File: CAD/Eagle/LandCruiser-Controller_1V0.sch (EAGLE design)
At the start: 56 parts, among them K311 V23086C1001A403, K312 V23086C1001A403, K313 V23086C1001A403, K314 V23086C1001A403, K315 V23086C1001A403, U101 MEGA8-P, U221 SN75240, U301 MIC2981/2982SO18W, U501 MAX232_SOIC16, U611 LM7805, X201 WEIDMUELLER 1234600000, X321 WEIDMUELLER 1234600000, X401 I2C

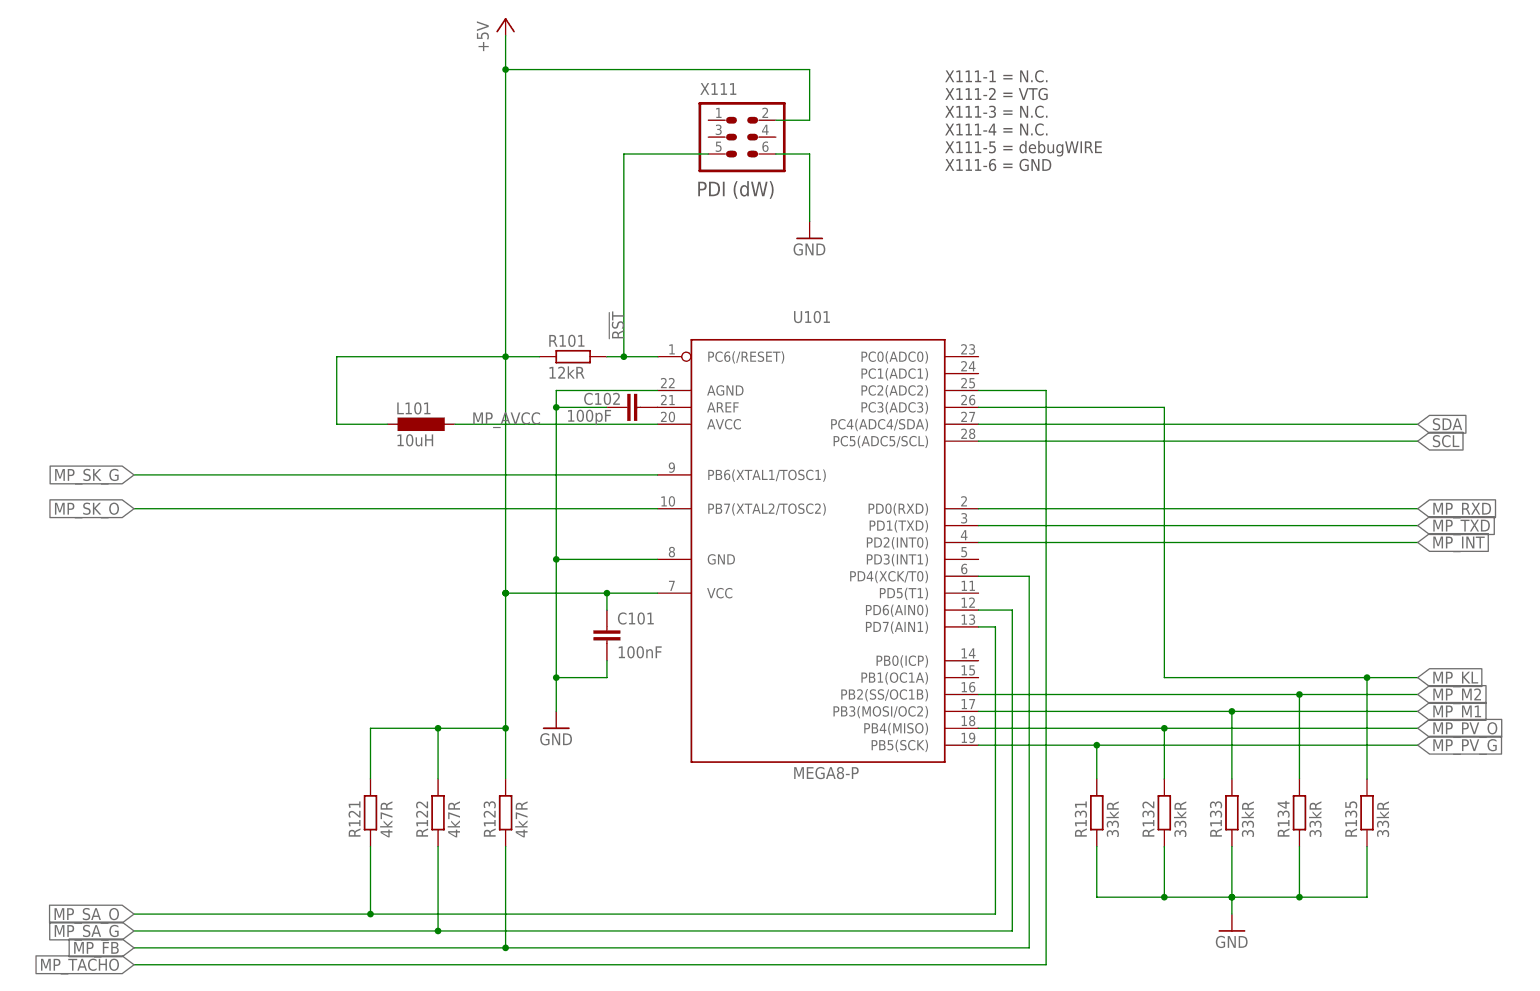
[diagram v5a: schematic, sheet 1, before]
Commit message: HW_V1.0 - Place&Routing - placement done, half of the routing done
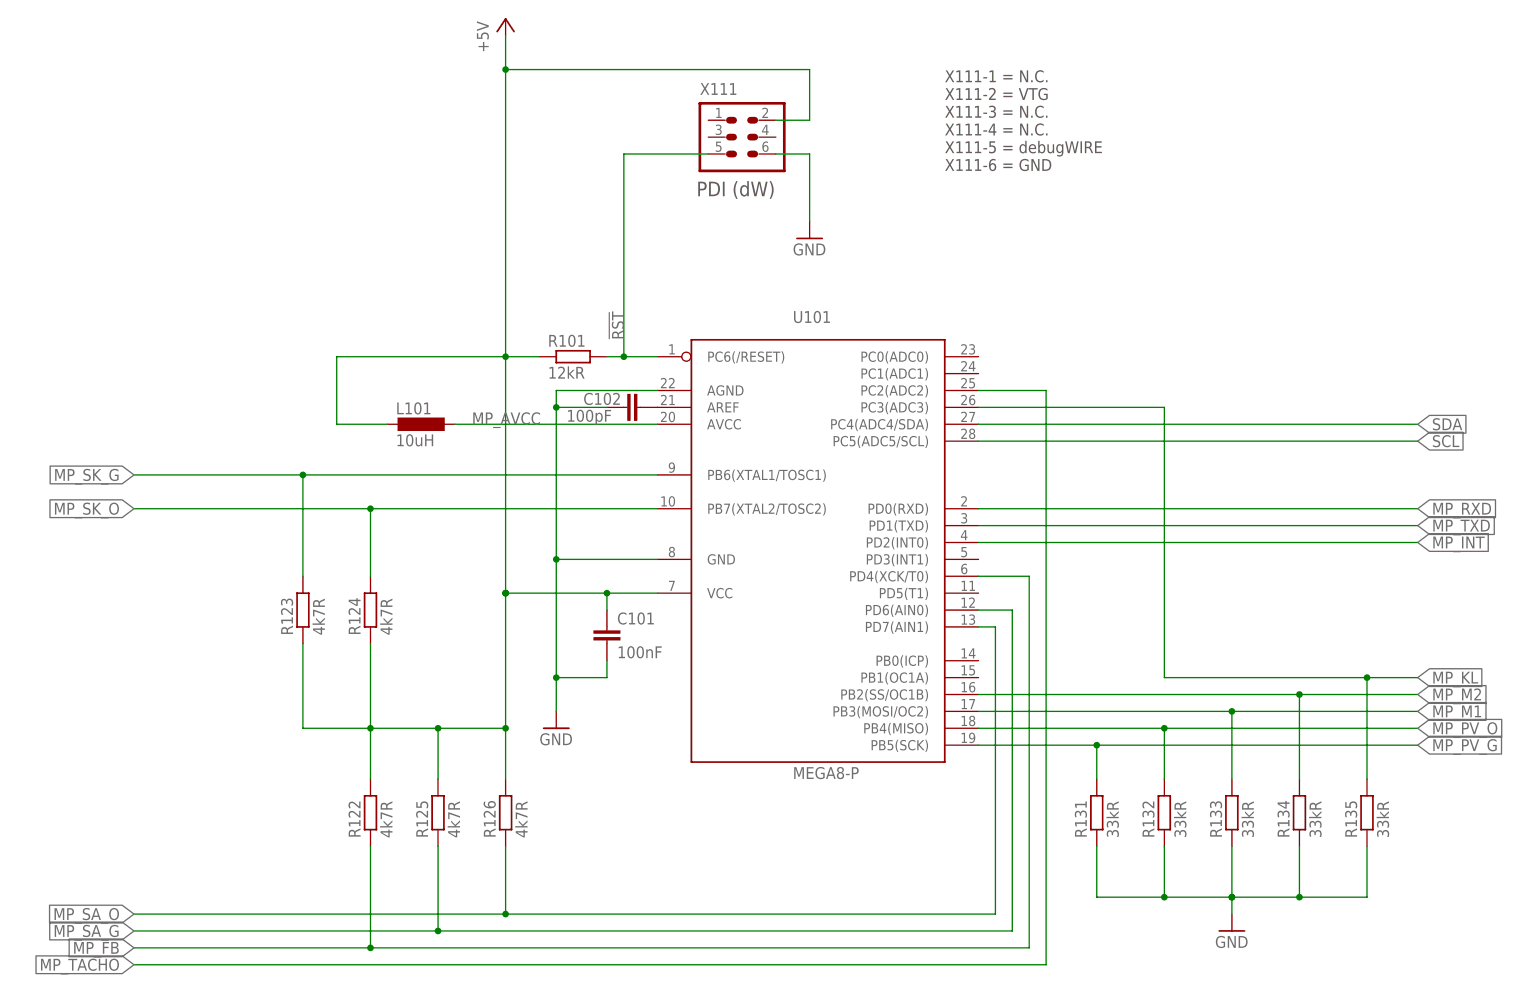
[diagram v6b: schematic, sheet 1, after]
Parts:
- removed R121: 4k7R, rcl:R-EU_R0805
- removed R232: 22kR, rcl:R-EU_R0805
- added R124, R125, R126: 4k7R, rcl:R-EU_R0805
- added R216: 56R, rcl:R-EU_R0805
- R211: value 56R -> 22kR
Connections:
- net +5V: now also R123.1, R124.1, R125.2, R126.2; no longer R121.2, R123.2
- net ECU_FB: now also R212.1; no longer R211.1
- net MP_FB: now also R122.1, R212.2; no longer R123.1, R211.2
- net MP_SA_G: now also R125.1, R215.2; no longer R122.1, R214.2
- net MP_SA_O: now also R126.1, R216.2; no longer R121.1, R215.2
- net MP_SK_G: now also R123.2, R213.2; no longer R212.2
- net MP_SK_O: now also R124.2, R214.2; no longer R213.2
- net MP_TACHO: now also R211.1; no longer R232.1
- net SA_G: now also R215.1; no longer R214.1
- net SA_O: now also R216.1; no longer R215.1
- net SK_G: now also R213.1; no longer R212.1
- net SK_O: now also R214.1; no longer R213.1
- net TACHO: now also R211.2; no longer R232.2
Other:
- moved on the sheet: R122, R123, R211, R212, R213, R214, R215

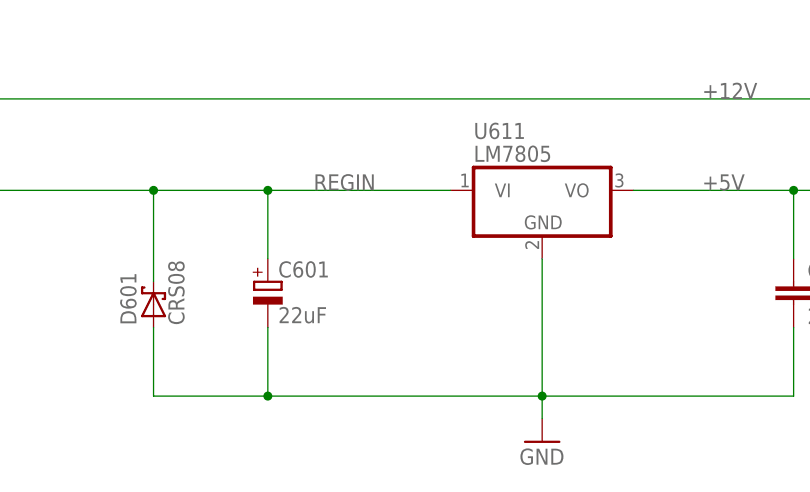
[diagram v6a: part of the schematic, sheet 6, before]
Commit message: HW_V1.0 - additional capacitors added
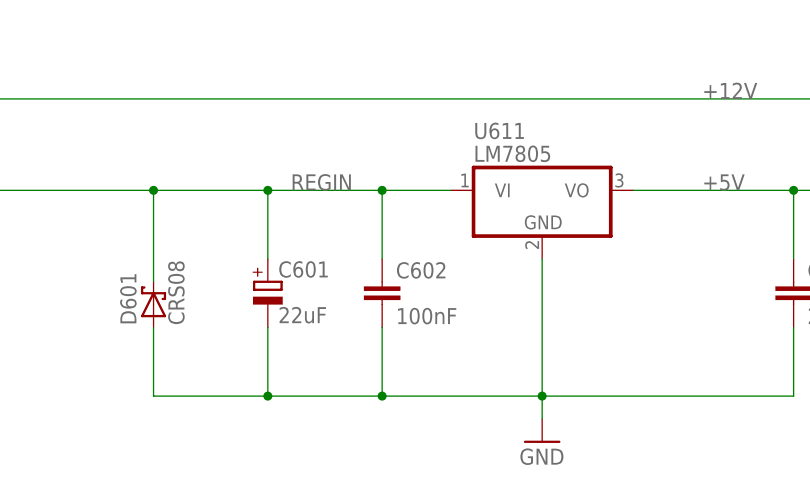
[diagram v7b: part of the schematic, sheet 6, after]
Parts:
- added C301, C602: 100nF, rcl:C-EUC0805
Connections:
- net +12V: now also C301.1
- net GND: now also C301.2, C602.2
- net REGIN: now also C602.1
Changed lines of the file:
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@@
 <part name="R123" library="rcl" deviceset="R-EU_" device="R0805" value="4k7R"/>
 <part name="R124" library="rcl" deviceset="R-EU_" device="R0805" value="4k7R"/>
+<part name="C602" library="rcl" deviceset="C-EU" device="C0805" value="100nF"/>
+<part name="C301" library="rcl" deviceset="C-EU" device="C0805" value="100nF"/>
 </parts>
 <sheets>
@@
 <instance part="GND314" gate="1" x="175.26" y="73.66"/>
 <instance part="GND315" gate="1" x="175.26" y="50.8"/>
+<instance part="C301" gate="G$1" x="40.64" y="134.62"/>
 </instances>
 <busses>
@@
 <wire x1="40.64" y1="73.66" x2="55.88" y2="73.66" width="0.1524" layer="91"/>
 <junction x="40.64" y="73.66"/>
+<pinref part="C301" gate="G$1" pin="2"/>
+<wire x1="40.64" y1="129.54" x2="40.64" y2="83.82" width="0.1524" layer="91"/>
+<junction x="40.64" y="83.82"/>
 </segment>
 <segment>
@@
 <wire x1="154.94" y1="58.42" x2="142.24" y2="58.42" width="0.1524" layer="91"/>
 <junction x="142.24" y="58.42"/>
+<pinref part="C301" gate="G$1" pin="1"/>
+<wire x1="40.64" y1="137.16" x2="40.64" y2="152.4" width="0.1524" layer="91"/>
+<wire x1="40.64" y1="152.4" x2="48.26" y2="152.4" width="0.1524" layer="91"/>
 </segment>
 </net>
@@
 <instance part="F601" gate="G$1" x="83.82" y="106.68"/>
 <instance part="F602" gate="G$1" x="83.82" y="96.52"/>
+<instance part="C602" gate="G$1" x="132.08" y="86.36"/>
 </instances>
 <busses>
@@
 <wire x1="149.86" y1="73.66" x2="177.8" y2="73.66" width="0.1524" layer="91"/>
 <junction x="149.86" y="73.66"/>
-<wire x1="149.86" y1="73.66" x2="119.38" y2="73.66" width="0.1524" layer="91"/>
+<wire x1="149.86" y1="73.66" x2="132.08" y2="73.66" width="0.1524" layer="91"/>
 <pinref part="C601" gate="G$1" pin="-"/>
+<wire x1="132.08" y1="73.66" x2="119.38" y2="73.66" width="0.1524" layer="91"/>
 <wire x1="119.38" y1="73.66" x2="119.38" y2="81.28" width="0.1524" layer="91"/>
 <pinref part="D601" gate="G$1" pin="A"/>
@@
 <junction x="119.38" y="73.66"/>
 <pinref part="U611" gate="A1" pin="GND"/>
+<pinref part="C602" gate="G$1" pin="2"/>
+<wire x1="132.08" y1="73.66" x2="132.08" y2="81.28" width="0.1524" layer="91"/>
+<junction x="132.08" y="73.66"/>
 </segment>
 </net>
@@
 <pinref part="C601" gate="G$1" pin="+"/>
 <pinref part="U611" gate="A1" pin="VI"/>
-<wire x1="119.38" y1="96.52" x2="139.7" y2="96.52" width="0.1524" layer="91"/>
+<wire x1="119.38" y1="96.52" x2="132.08" y2="96.52" width="0.1524" layer="91"/>
+<wire x1="132.08" y1="96.52" x2="139.7" y2="96.52" width="0.1524" layer="91"/>
 <wire x1="119.38" y1="96.52" x2="119.38" y2="88.9" width="0.1524" layer="91"/>
 <junction x="119.38" y="96.52"/>
@@
 <junction x="106.68" y="96.52"/>
 <wire x1="88.9" y1="96.52" x2="106.68" y2="96.52" width="0.1524" layer="91"/>
-<label x="124.46" y="96.52" size="1.778" layer="95"/>
+<label x="121.92" y="96.52" size="1.778" layer="95"/>
 <pinref part="F602" gate="G$1" pin="2"/>
-</segment>
-</net>
+<pinref part="C602" gate="G$1" pin="1"/>
+<wire x1="132.08" y1="96.52" x2="132.08" y2="88.9" width="0.1524" layer="91"/>
+<junction x="132.08" y="96.52"/>
+</segment>
+</net>
